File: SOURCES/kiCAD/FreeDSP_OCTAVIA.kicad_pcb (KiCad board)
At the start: 4 copper layers, 178 x 99 mm, 513 parts, among them IC1 TPS5430DDA, IC2 PCM1808QPWRQ1, J1 Conn_01x08, J10 Conn_01x02, J11 Conn_Coaxial, J12 IDC_2x5, J13 Conn_01x05, J16 MJ-519, J17 MJ-519, J2 DC7.5V-9V IN, J20 MJ-519, J21 MJ-519, J24 Conn_01x06, J25 Conn_01x06, J27 Conn_01x06, J28 Conn_01x06, J3 Conn_01x08, J4 Header_01x06, J5 MJ-519, J6 8P_DIP_SOCKET, J7 Header_01x04, J8 Header_01x04, J9 Conn_01x02, P1 Conn_02x20_Odd_Even, Q1 AO3401A, Q10 2SC3326, Q11 2SC3326, Q12 MJD45H11T4, Q13 2N7002, Q14 2N7002, Q15 2SC3326, Q16 2SC3326, Q17 2SC3326, Q18 2SC3326, Q19 2SC3326, Q2 MMBT5401, Q20 2SC3326, Q21 2SC3326, Q22 2SC3326, Q23 2SC3326, Q24 2SC3326, Q25 2SC3326, Q26 2SC3326, Q27 2SC3326, Q28 2SC3326, Q29 AO3401A, Q3 2N7002, Q30 2N7002, Q31 2N7002, Q32 2N7002, Q4 MMBT5401, Q5 AO3401A, Q6 2N7002, Q7 AO3401A, Q8 2N7002, Q9 2N7002, SW1 SW_Push, SW2 SW_SPDT, SW3 SW_SPDT, SW4 SW_NOP_DPDT, SW7 DSP_RES, T1 PE-65612NL, U1 GP1UXC41QS, U10 74LVC1G86, U11 74LVC1G04, U12 ADAU1452, U13 25AA1024, U14 PCM5102A, U15 74LVC1G04, U16 PCM5102A, U17 PCM5102A, U18 PCM5102A, U2 PLR135-T10, U20 OPA1632DR, U21 OPA1632DR, U22 OPA1632DR, U23 OPA1632DR, U24 OPA1632DR, U25 OPA1632DR, U26 OPA1632DR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

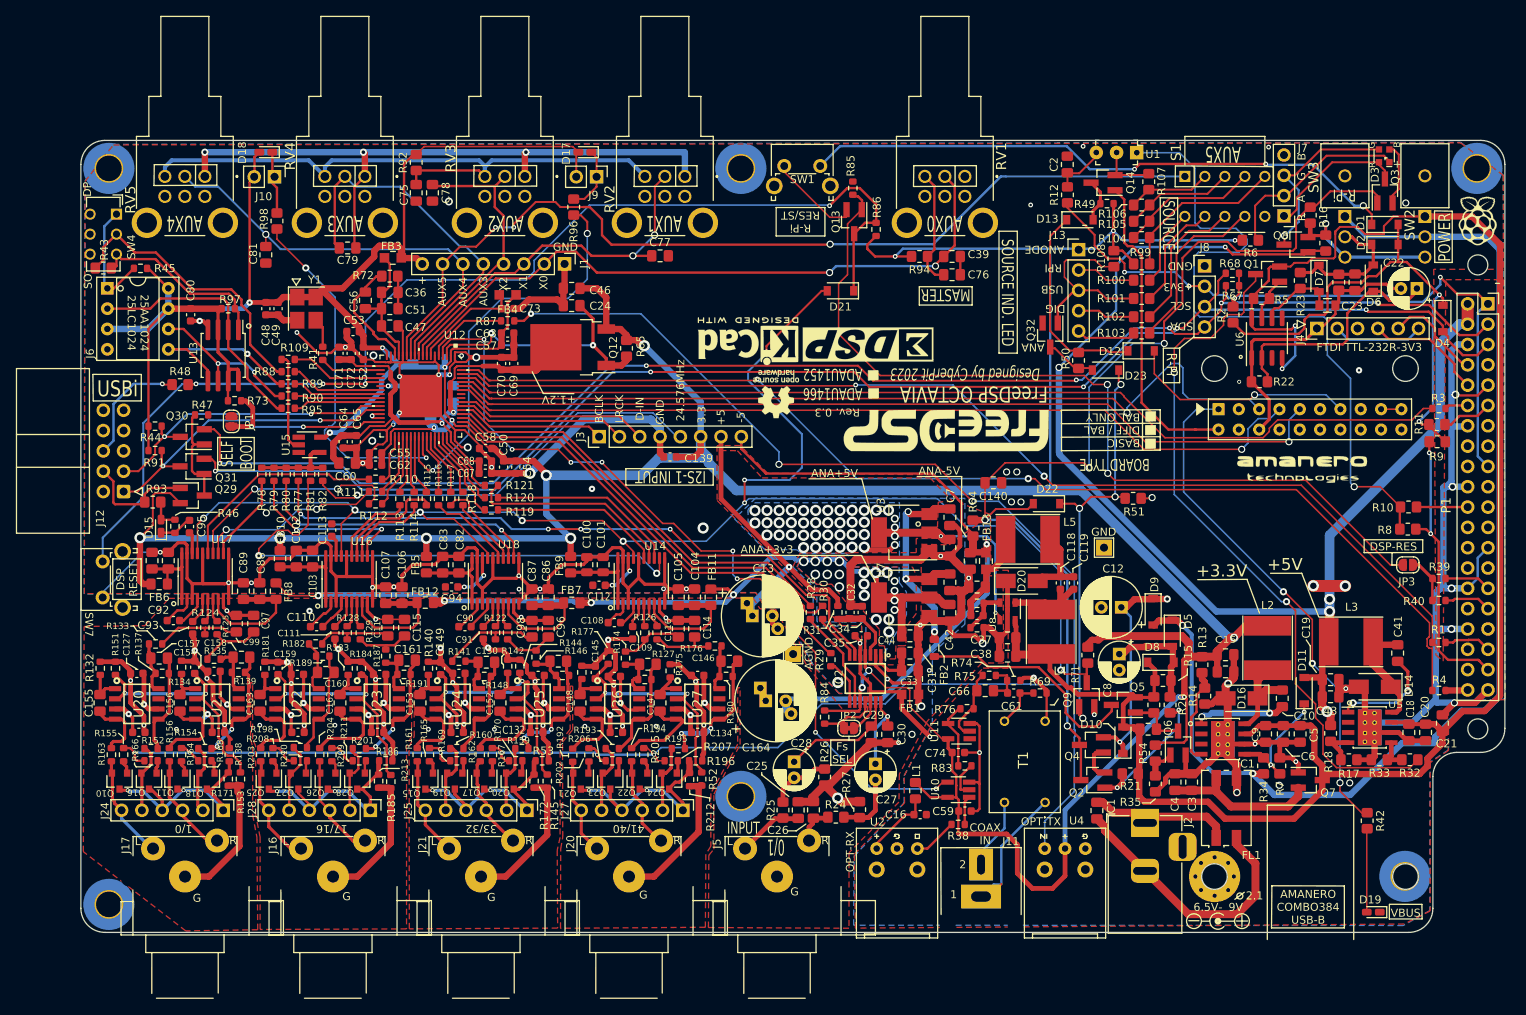
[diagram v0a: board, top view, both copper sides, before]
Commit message: Improved Coax Input Noise Immunities
Changed Coax input amp design and AC couling to EXOR
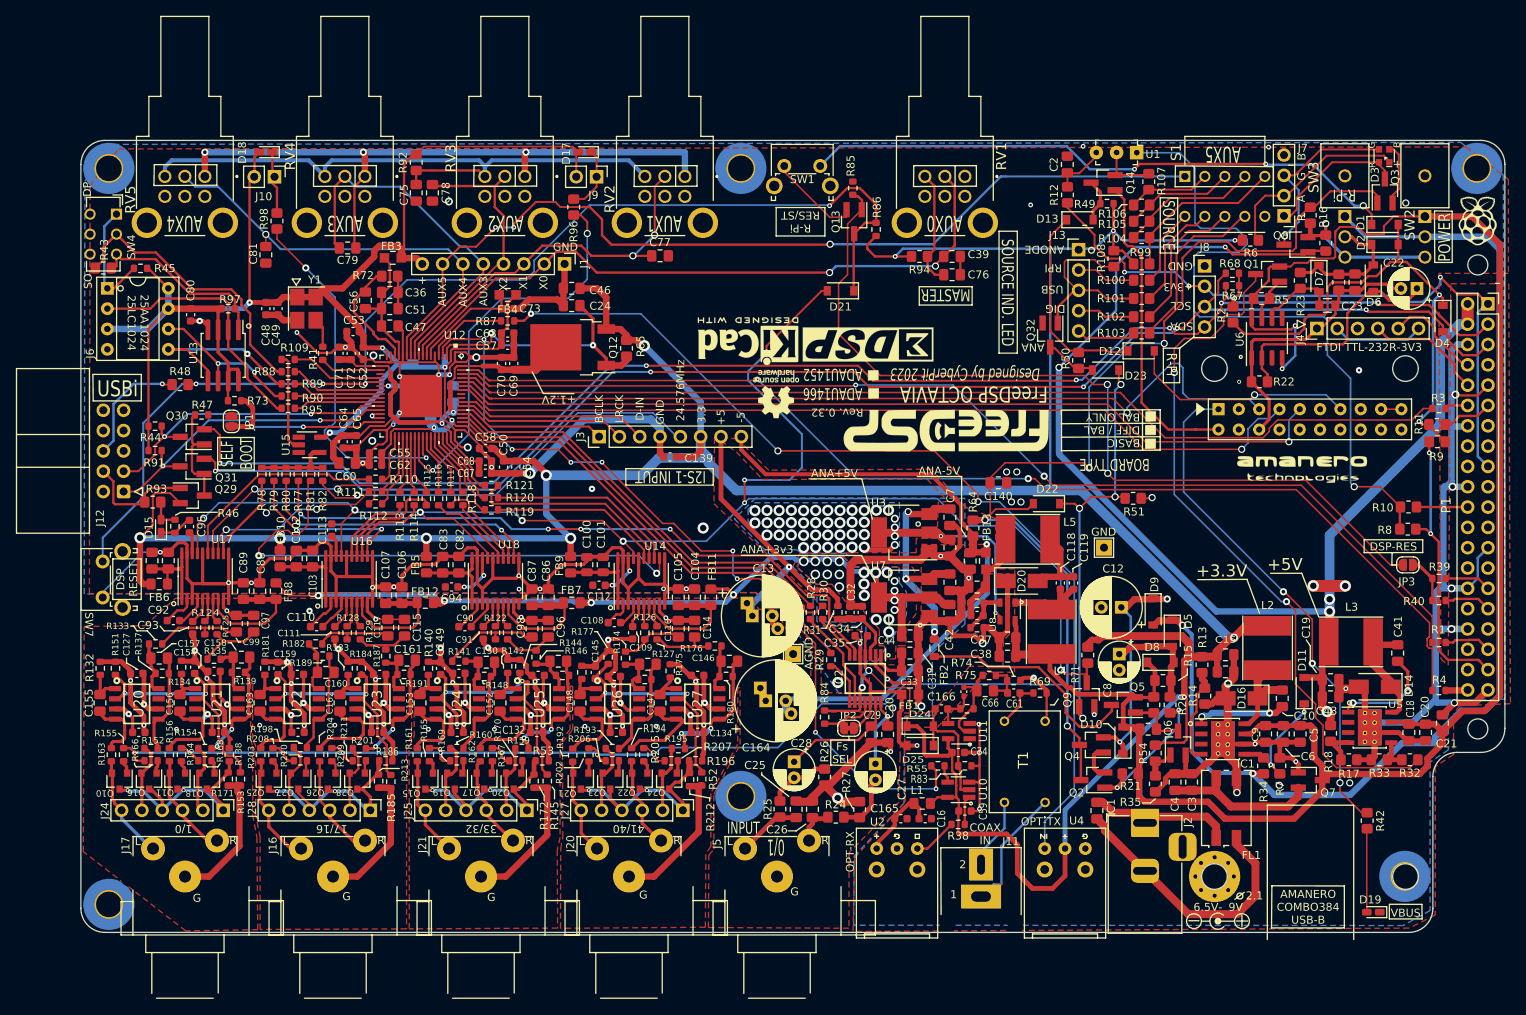
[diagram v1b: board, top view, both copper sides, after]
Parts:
- added C165: 10uF, Capacitor_SMD:C_0603_1608Metric, F.Cu at (132.5, 135.8)
- added C166: 2.2pF, Capacitor_SMD:C_0402_1005Metric_Pad0.74x0.62mm_HandSolder, F.Cu at (140.4, 119.9)
- added C167: 0.1uF, Capacitor_SMD:C_0603_1608Metric, F.Cu at (137.6, 122.1)
- added D24: SS2040FL, Diode_SMD:D_SOD-123, F.Cu at (134.9, 124.2)
- added D25: SS2040FL, Diode_SMD:D_SOD-123, F.Cu at (134.9, 126.6)
- added R55: 47R, Resistor_SMD:R_0603_1608Metric, F.Cu at (137.1, 129.2)
- R38: value 33R -> 0R
- R69, R75: value 75R -> 150R
- R76: value 330R -> 560R
- R83: value 33R -> 1k
- moved L1 1.81 mm to (135.2, 133.9), turned to 0 degrees
- moved C16 0.81 mm to (135.5, 135.8)
- moved C140 0.63 mm to (144.7, 93.8)
- moved R25 0.40 mm to (117.4, 134.6)
- moved C25 0.27 mm to (119.4, 134.6)
- moved C26 0.15 mm to (121.4, 134.6)
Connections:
- R76 pad 2: Net-(R76-Pad2) -> Net-(C166-Pad1)
- R83 pad 1: Net-(R83-Pad1) -> GND
- R83 pad 2: Net-(R76-Pad2) -> Net-(C167-Pad2)
- U10 pad 2: Net-(R83-Pad1) -> Net-(C167-Pad2)
- U10 pad 4: /ADC_IO Part/958RX -> Net-(R55-Pad2)
- U11 pad 4: Net-(R76-Pad2) -> Net-(C166-Pad1)
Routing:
- net Net-(C167-Pad2): track 0.00 -> 16.3 mm
- net Net-(R76-Pad2): track 8.42 -> 0.00 mm
- net Net-(C166-Pad1): track 0.00 -> 5.26 mm
- net Net-(R83-Pad1): track 4.65 -> 0.00 mm
- net GND: track 695.0 -> 697.9 mm, vias 69 -> 71
- net +3V3: track 696.6 -> 699.3 mm
- net Net-(R55-Pad2): track 0.00 -> 2.19 mm
- net Net-(C166-Pad2): track 9.34 -> 11.0 mm
- net Net-(C16-Pad1): track 8.83 -> 10.2 mm
- net /ADC_IO Part/958RX: track 103.2 -> 104.5 mm
- net -5VA: track 355.0 -> 353.9 mm
- net Net-(C27-Pad2): track 8.16 -> 7.58 mm
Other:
- board text added: "Rev. 0.32"
- board text removed: "Rev. 0.3"

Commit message: Voltage Regulator Changed to LM317
PCB layout is also updated in some of the places.
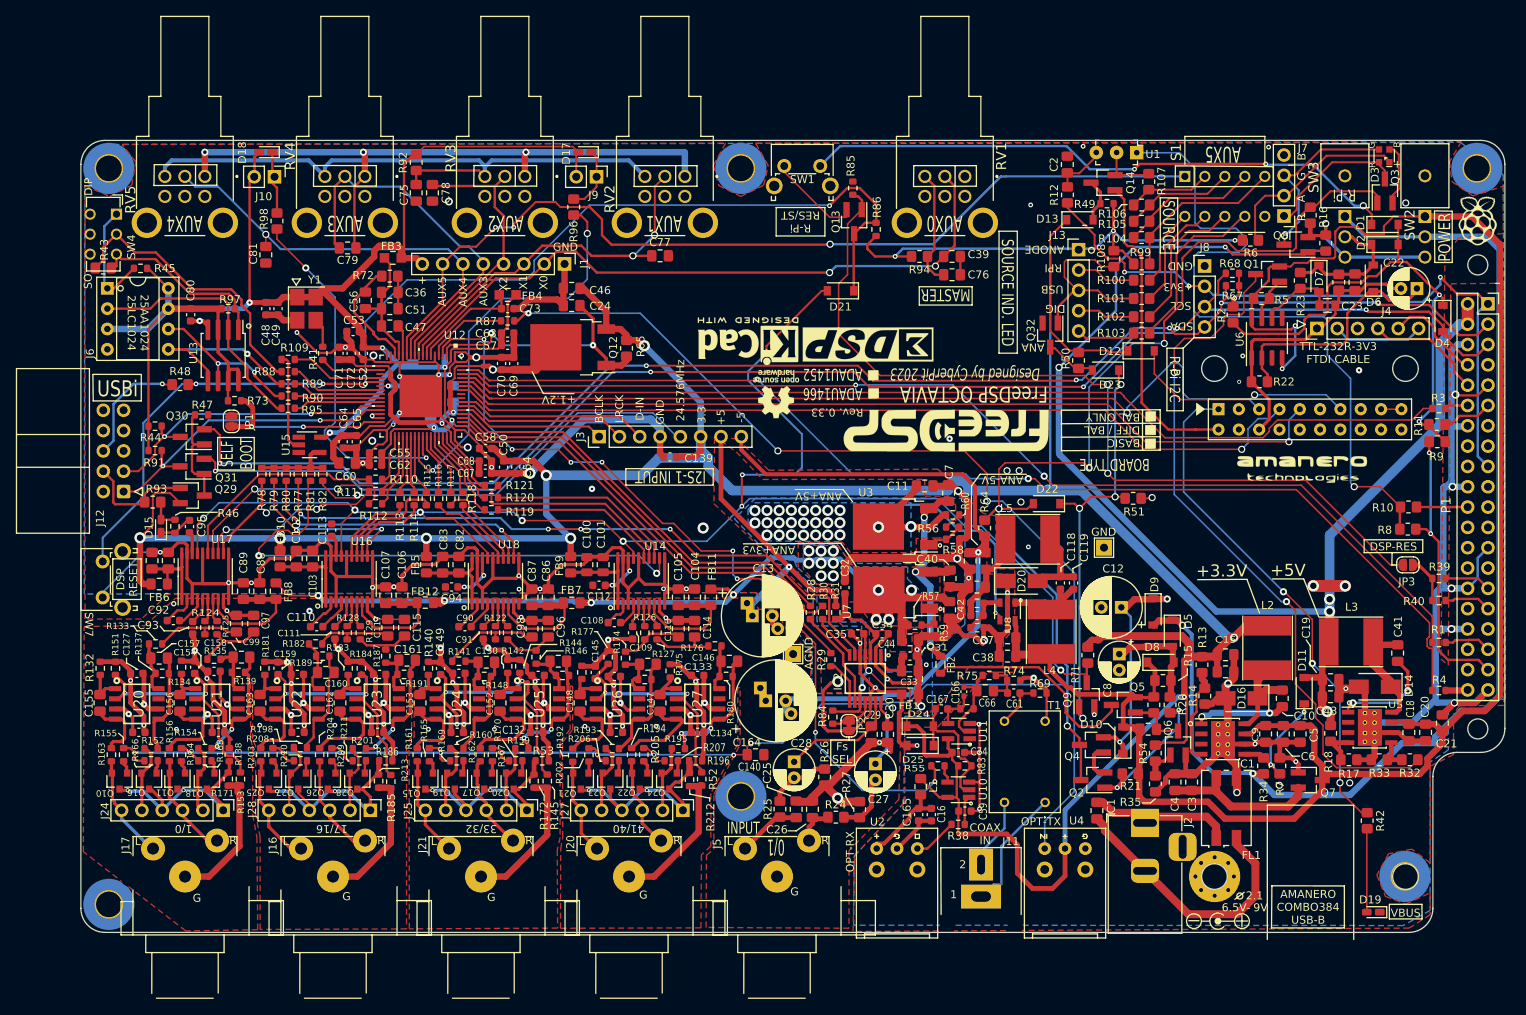
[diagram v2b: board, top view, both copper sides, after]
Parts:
- added R56: 100R, Resistor_SMD:R_0603_1608Metric, F.Cu at (139.0, 99.3)
- added R57: 120R, Resistor_SMD:R_0603_1608Metric, F.Cu at (134.3, 111.6)
- added R58: 330R, Resistor_SMD:R_0603_1608Metric, F.Cu at (139.0, 100.9)
- added R59: 200R, Resistor_SMD:R_0603_1608Metric, F.Cu at (136.6, 112.2)
- added R60: 10R, Resistor_SMD:R_0603_1608Metric, F.Cu at (139.0, 97.8)
- C114, C115, C116, C117, C96, C97, C98, C99: value 10nF(C0G) -> 4.7nF(C0G)
- C31: footprint Capacitor_SMD:C_0805_2012Metric_Pad1.18x1.45mm_HandSolder -> Capacitor_SMD:C_0603_1608Metric_Pad1.08x0.95mm_HandSolder
- R122, R123, R124, R125, R126, R127, R128, R129: value 220R -> 470R
- U3: value AMS1117-5.0 -> LM317AG-TN3-R; footprint Package_TO_SOT_SMD:SOT-223-3_TabPin2 -> Package_TO_SOT_SMD:TO-252-2
- U7: value AMS1117-3.3 -> LM317AG-TN3-R; footprint Package_TO_SOT_SMD:SOT-223-3_TabPin2 -> Package_TO_SOT_SMD:TO-252-2
- moved C140 45.6 mm to (114.3, 127.8)
- moved C11 8.34 mm to (135.5, 94.2), turned to 0 degrees
- moved C34 3.64 mm to (130.1, 112.7), turned to 0 degrees
- moved C32 3.18 mm to (125.5, 106.9)
- moved C7 3.03 mm to (138.5, 95.1), turned to 90 degrees
- moved C165 2.28 mm to (134.7, 135.3), turned to 270 degrees
- moved FB2 2.23 mm to (137.4, 116.5)
- moved L1 2.10 mm to (135.0, 131.8), turned to 90 degrees
- moved R64 1.46 mm to (143.0, 99.5)
- moved U7 1.40 mm to (131.9, 107.2)
- moved U3 1.33 mm to (131.8, 99.3)
- moved R84 1.02 mm to (124.0, 123.1)
- moved C16 0.92 mm to (136.3, 135.3), turned to 270 degrees
- moved C35 0.51 mm to (127.1, 112.7)
- moved C44 0.51 mm to (133.6, 113.4)
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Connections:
- C140 pad 1: GND -> GNDA
- R83 pad 1: GND -> +3V3
- U3 pad 1: GNDA -> Net-(R56-Pad2)
- U7 pad 1: GNDA -> Net-(R57-Pad2)
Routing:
- net GND: track 697.9 -> 714.9 mm, vias 71 -> 72
- net +5VA: track 357.6 -> 370.6 mm, vias 52 -> 35
- net /ADC_IO Part/DVDD: track 64.1 -> 73.8 mm, vias 2 -> 3
- net +3.3VA: track 105.1 -> 110.6 mm, vias 24 -> 16
- net MUTE: track 280.4 -> 274.9 mm, vias 12 -> 14
- net +3V3: track 699.3 -> 704.1 mm
- net Net-(R56-Pad2): track 0.00 -> 4.58 mm
- net Net-(R57-Pad2): track 0.00 -> 3.95 mm
- net GNDA: track 269.2 -> 272.9 mm, vias 44 -> 46
- net -5VA: track 353.9 -> 357.2 mm
- net Net-(C32-Pad1): track 8.61 -> 11.8 mm
- net Net-(R56-Pad1): track 0.00 -> 2.28 mm
- net Net-(C16-Pad1): track 10.2 -> 12.1 mm
- net /ADC_IO Part/958TX: track 120.0 -> 121.8 mm
- net Net-(C40-Pad1): track 29.0 -> 27.6 mm
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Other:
- board text added: "0"
- board text added: "1"
- board text added: "16"
- board text added: "17"
- board text added: "32"
- board text added: "33"
- board text added: "41"
- board text added: "DIP"
- board text added: "R-Pi I2C"
- board text added: "Rev. 0.33"
- board text added: "TTL-232R-3V3 FTDI CABLE"
- board text removed: "DP"
- board text removed: "FTDI TTL-232R-3V3"
- board text removed: "Rev. 0.32"

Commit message: Released for everyone, ready to build.
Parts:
- removed Q14: 2N7002, Package_TO_SOT_SMD:SOT-23_Handsoldering
- added C168: 10uF, Capacitor_SMD:C_0805_2012Metric_Pad1.18x1.45mm_HandSolder, F.Cu at (129.6, 69.7)
- added R61: 0R, Resistor_SMD:R_0603_1608Metric, F.Cu at (122.6, 117.2)
- A1: value Combo384 -> Combo384-Combo384
- J16, J17, J20, J21, J5: value MJ-519 -> RCJ-2223; footprint MyJacks:MJ-519 -> MyJacks:RCJ-2223
- R49: value 3.3k -> 10k
- R57: value 120R -> 180R
- R59: value 200R -> 270R
- R74: value 4.7k -> 100k
- R76: value 560R -> 1.2k
- moved R29 0.43 mm to (123.5, 115.5), turned to 180 degrees
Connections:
- D13 pad 2: Net-(D13-Pad2) -> Net-(A1-Pad11)
- J17 pad 1: /ADC_IO Part/DAC/OUT0_P -> /ADC_IO Part/DAC/OUT1_P
- J17 pad 2: /ADC_IO Part/DAC/OUT1_P -> /ADC_IO Part/DAC/OUT0_P
- J24 pad 3: /ADC_IO Part/DAC/OUT0_P -> /ADC_IO Part/DAC/OUT1_P
- J24 pad 6: /ADC_IO Part/DAC/OUT1_P -> /ADC_IO Part/DAC/OUT0_P
- Q10 pad 2: /ADC_IO Part/DAC/OUT1_P -> /ADC_IO Part/DAC/OUT0_P
- Q11 pad 2: /ADC_IO Part/DAC/OUT0_P -> /ADC_IO Part/DAC/OUT1_P
- R155 pad 2: /ADC_IO Part/DAC/OUT1_P -> /ADC_IO Part/DAC/OUT0_P
- R156 pad 1: /ADC_IO Part/DAC/OUT0_P -> /ADC_IO Part/DAC/OUT1_P
- R49 pad 1: Net-(D13-Pad2) -> GND
- R49 pad 2: +3V3 -> Net-(A1-Pad11)
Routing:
- net GND: track 714.9 -> 724.0 mm, vias 72 -> 78
- net /ADC_IO Part/DAC/OUT16_P: track 12.5 -> 21.3 mm
- net Net-(C26-Pad1): track 4.91 -> 13.4 mm, vias 0 -> 1
- net /ADC_IO Part/DAC/OUT0_P: track 13.4 -> 21.1 mm
- net /ADC_IO Part/DAC/OUT32_P: track 12.9 -> 19.7 mm
- net /ADC_IO Part/DAC/OUT40_P: track 12.3 -> 18.8 mm
- net Net-(D13-Pad2): track 5.50 -> 0.00 mm
- net GNDA: track 272.9 -> 276.9 mm
- net +3V3: track 704.1 -> 700.8 mm
- net /ADC_IO Part/DAC/OUT41_P: track 11.6 -> 14.4 mm
- net /ADC_IO Part/DAC/OUT33_P: track 12.0 -> 14.2 mm
- net ~DSP-RESET: track 145.3 -> 147.3 mm
- net Net-(A1-Pad11): track 39.3 -> 41.1 mm
- net /ADC_IO Part/DAC/DIFF_GND2: track 17.8 -> 19.4 mm
- net /ADC_IO Part/DAC/DIFF_GND3: track 18.5 -> 19.6 mm
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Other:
- board text added: "16/17"
- board text added: "32/33"
- board text added: "40/41"
- board text added: "Rev. 1.00"
- board text removed: "1/0"
- board text removed: "17/16"
- board text removed: "33/32"
- board text removed: "41/40"
- board text removed: "Rev. 0.33"
